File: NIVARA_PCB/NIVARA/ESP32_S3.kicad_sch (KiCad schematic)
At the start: 0 parts

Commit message: SALIDAS DE VOLTAJE Y CORRIENTE
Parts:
- added U11: ESP32-S3-WROOM-1, PCM_Espressif:ESP32-S3-WROOM-1, symbol PCM_Espressif:ESP32-S3-WROOM-1
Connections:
- new net: U11.1 (GND), U11.40 (GND), U11.41 (GND)

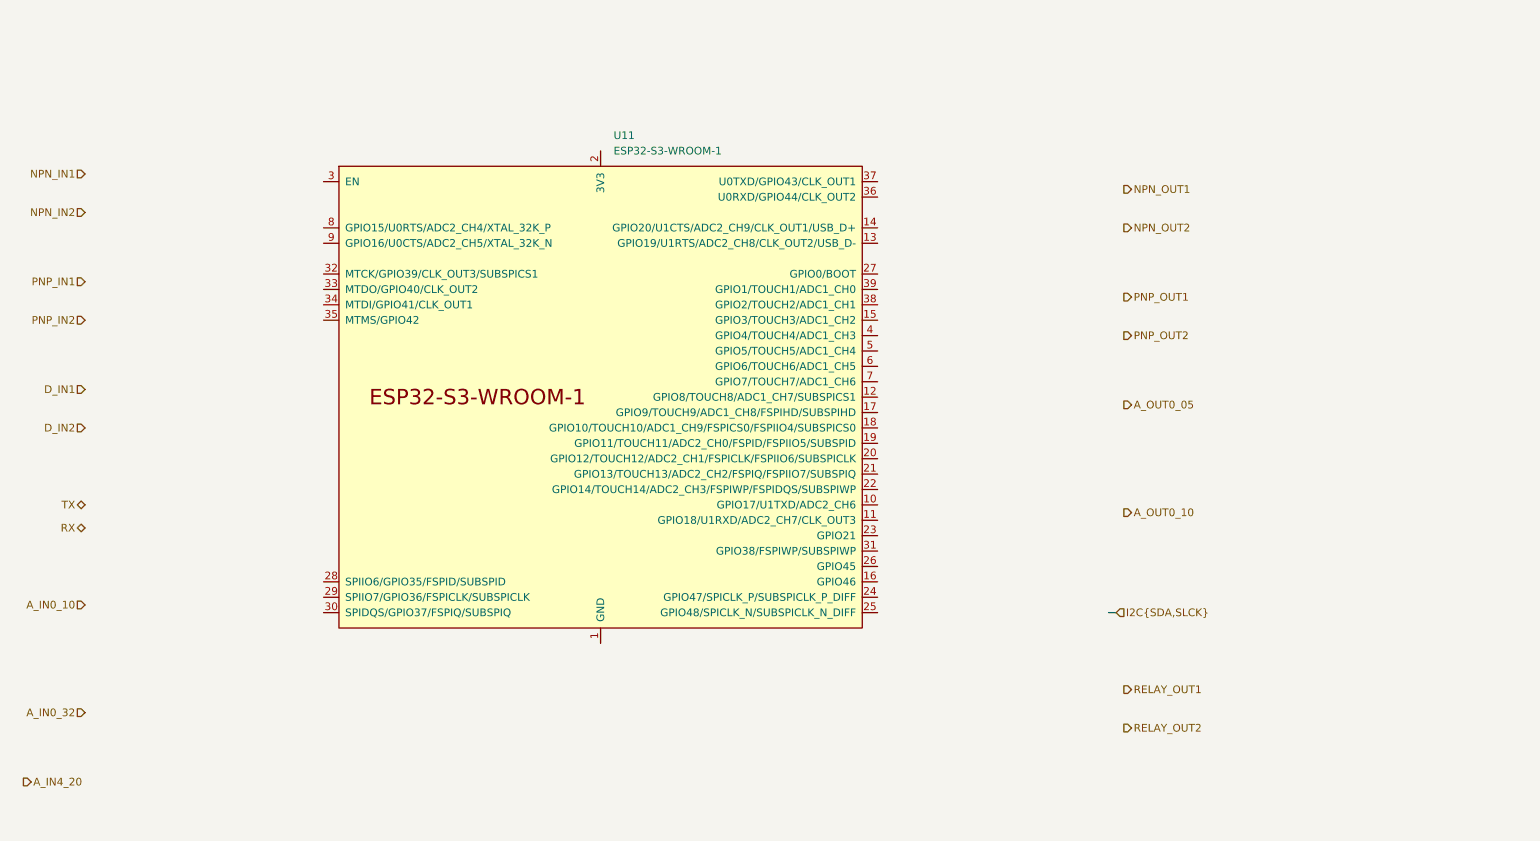
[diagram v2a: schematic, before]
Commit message: Se organizaron componentes en el area de PCB
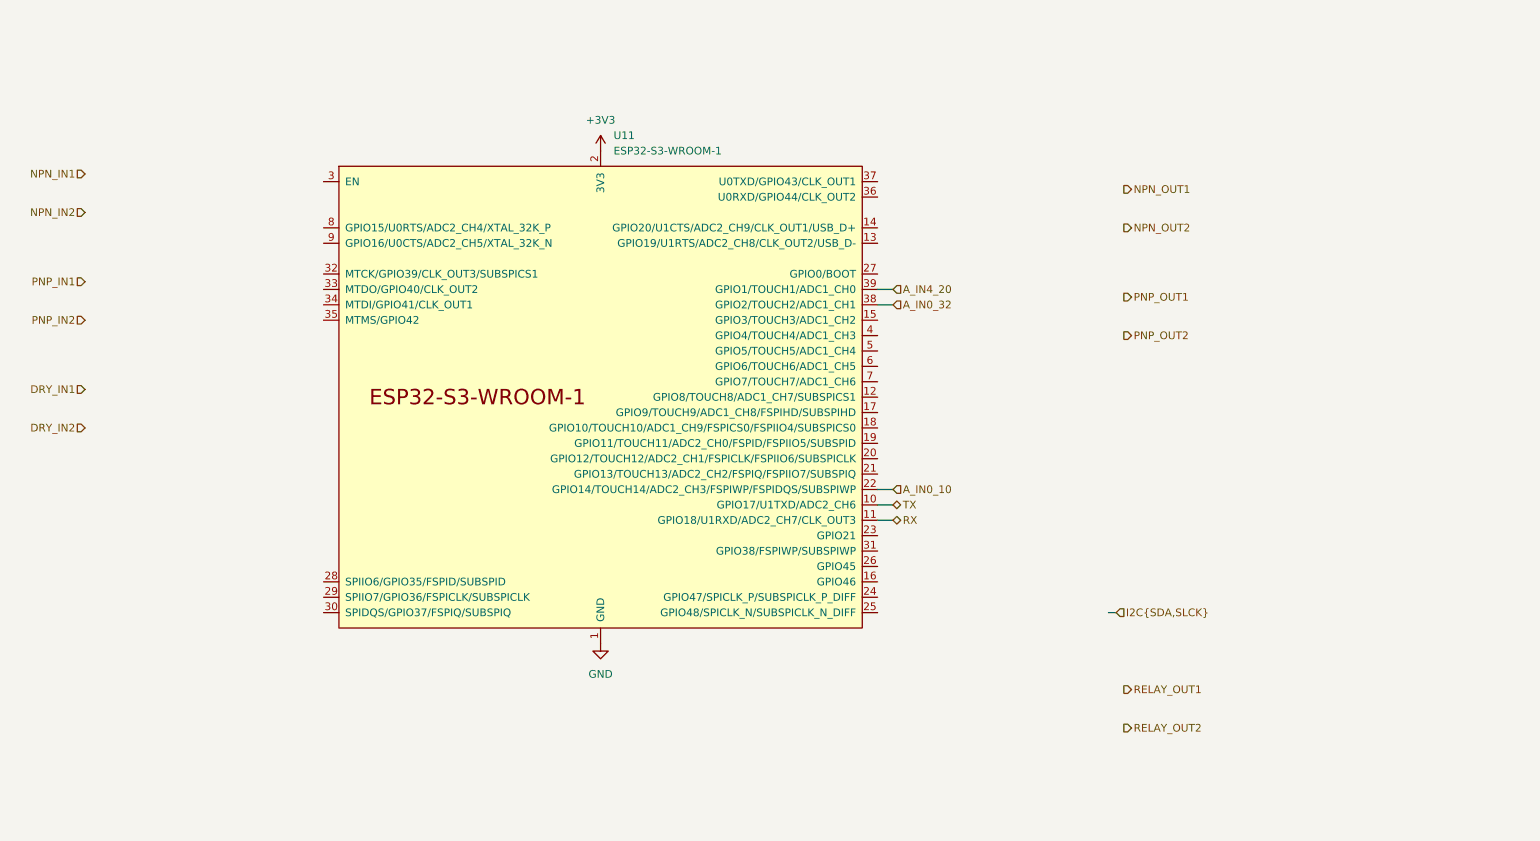
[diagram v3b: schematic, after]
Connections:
- net A_IN0_10: now also U11.22 (GPIO14/TOUCH14/ADC2_CH3/FSPIWP/FSPIDQS/SUBSPIWP)
- net A_IN0_32: now also U11.38 (GPIO2/TOUCH2/ADC1_CH1)
- net A_IN4_20: now also U11.39 (GPIO1/TOUCH1/ADC1_CH0)
- net RX: now also U11.11 (GPIO18/U1RXD/ADC2_CH7/CLK_OUT3)
- net TX: now also U11.10 (GPIO17/U1TXD/ADC2_CH6)
- net GND: now reaches U11.1 (GND), U11.40 (GND), U11.41 (GND)
- net +3V3: now reaches U11.2 (3V3)
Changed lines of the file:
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@@
+		)
+	)
+	(wire
+		(pts
+			(xy 158.75 64.77) (xy 161.29 64.77)
+		)
+		(stroke
+			(width 0)
+			(type default)
+		)
+	)
+	(wire
+		(pts
+			(xy 158.75 97.79) (xy 161.29 97.79)
+		)
+		(stroke
+			(width 0)
+			(type default)
+		)
+	)
+	(wire
+		(pts
+			(xy 158.75 100.33) (xy 161.29 100.33)
+		)
+		(stroke
+			(width 0)
+			(type default)
+		)
+	)
+	(wire
+		(pts
+			(xy 158.75 102.87) (xy 161.29 102.87)
+		)
+		(stroke
+			(width 0)
+			(type default)
+		)
+	)
+	(wire
+		(pts
+			(xy 158.75 67.31) (xy 161.29 67.31)
+		)
+		(stroke
+			(width 0)
+			(type default)
 		)
 	)
@@
 		)
 	)
-	(hierarchical_label "D_IN2"
+	(hierarchical_label "DRY_IN2"
 		(shape input)
 		(at 27.94 87.63 180)
@@
 	(hierarchical_label "RX"
 		(shape bidirectional)
-		(at 27.94 104.14 180)
-		(effects
-			(font
-				(size 1.27 1.27)
-			)
-			(justify right)
+		(at 161.29 102.87 0)
+		(effects
+			(font
+				(size 1.27 1.27)
+			)
+			(justify left)
 		)
 	)
 	(hierarchical_label "A_IN4_20"
-		(shape output)
-		(at 17.78 146.05 0)
+		(shape input)
+		(at 161.29 64.77 0)
 		(effects
 			(font
@@
 		)
 	)
-	(hierarchical_label "A_OUT0_05"
-		(shape output)
-		(at 199.39 83.82 0)
-		(effects
-			(font
-				(size 1.27 1.27)
-			)
-			(justify left)
-		)
-	)
 	(hierarchical_label "NPN_IN1"
 		(shape input)
@@
 		)
 	)
-	(hierarchical_label "A_OUT0_10"
-		(shape output)
-		(at 199.39 101.6 0)
-		(effects
-			(font
-				(size 1.27 1.27)
-			)
-			(justify left)
-		)
-	)
 	(hierarchical_label "RELAY_OUT1"
 		(shape output)
@@
 	(hierarchical_label "A_IN0_32"
 		(shape input)
-		(at 27.94 134.62 180)
-		(effects
-			(font
-				(size 1.27 1.27)
-			)
-			(justify right)
+		(at 161.29 67.31 0)
+		(effects
+			(font
+				(size 1.27 1.27)
+			)
+			(justify left)
 		)
 	)
@@
 		)
 	)
-	(hierarchical_label "D_IN1"
+	(hierarchical_label "DRY_IN1"
 		(shape input)
 		(at 27.94 81.28 180)
@@
 	(hierarchical_label "A_IN0_10"
 		(shape input)
-		(at 27.94 116.84 180)
-		(effects
-			(font
-				(size 1.27 1.27)
-			)
-			(justify right)
+		(at 161.29 97.79 0)
+		(effects
+			(font
+				(size 1.27 1.27)
+			)
+			(justify left)
 		)
 	)
 	(hierarchical_label "TX"
 		(shape bidirectional)
-		(at 27.94 100.33 180)
-		(effects
-			(font
-				(size 1.27 1.27)
-			)
-			(justify right)
+		(at 161.29 100.33 0)
+		(effects
+			(font
+				(size 1.27 1.27)
+			)
+			(justify left)
 		)
 	)
@@
 					(unit 1)
 				)
+			)
+		)
+	)
+	(symbol
+		(lib_id "power:+3V3")
+		(at 113.03 41.91 0)
+		(unit 1)
+		(exclude_from_sim no)
+		(in_bom yes)
+		(on_board yes)
+		(dnp no)
+		(fields_autoplaced yes)
+		(property "Reference" "#PWR02"
+			(at 113.03 45.72 0)
+			(effects
+				(font
+					(size 1.27 1.27)
+				)
+				(hide yes)
+			)
+		)
+		(property "Value" "+3V3"
+			(at 113.03 36.83 0)
+			(effects
+				(font
+					(size 1.27 1.27)
+				)
+			)
+		)
+		(property "Footprint" ""
+			(at 113.03 41.91 0)
+			(effects
+				(font
+					(size 1.27 1.27)
+				)
+				(hide yes)
+			)
+		)
+		(property "Datasheet" ""
+			(at 113.03 41.91 0)
+			(effects
+				(font
+					(size 1.27 1.27)
+				)
+				(hide yes)
+			)
+		)
+		(property "Description" "Power symbol creates a global label with name \"+3V3\""
+			(at 113.03 41.91 0)
+			(effects
+				(font
+					(size 1.27 1.27)
+				)
+				(hide yes)
+			)
+		)
+		(pin "1"
+		)
+		(instances
+			(project ""
+				(path "/6298d7d5-28da-40bf-9586-24a8e5c02b82/7ff0dada-fc46-483c-91ad-b264be8c64cf/f3254285-1e0e-4dcc-8694-b92c90374f4d"
+					(reference "#PWR02")
+					(unit 1)
+				)
+			)
+		)
+	)
+	(symbol
+		(lib_id "power:GND")
+		(at 113.03 123.19 0)
+		(unit 1)
+		(exclude_from_sim no)
+		(in_bom yes)
+		(on_board yes)
+		(dnp no)
+		(fields_autoplaced yes)
+		(property "Reference" "#PWR086"
+			(at 113.03 129.54 0)
+			(effects
+				(font
+					(size 1.27 1.27)
+				)
+				(hide yes)
+			)
+		)
+		(property "Value" "GND"
+			(at 113.03 128.27 0)
+			(effects
+				(font
+					(size 1.27 1.27)
+				)
+			)
+		)
+		(property "Footprint" ""
+			(at 113.03 123.19 0)
+			(effects
+				(font
+					(size 1.27 1.27)
+				)
+				(hide yes)
+			)
+		)
+		(property "Datasheet" ""
+			(at 113.03 123.19 0)
+			(effects
+				(font
+					(size 1.27 1.27)
+				)
+				(hide yes)
+			)
+		)
+		(property "Description" "Power symbol creates a global label with name \"GND\" , ground"
+			(at 113.03 123.19 0)
+			(effects
+				(font
+					(size 1.27 1.27)
+				)
+				(hide yes)
+			)
+		)
+		(pin "1"
+		)
+		(instances
+			(project ""
+				(path "/6298d7d5-28da-40bf-9586-24a8e5c02b82/7ff0dada-fc46-483c-91ad-b264be8c64cf/f3254285-1e0e-4dcc-8694-b92c90374f4d"
+					(reference "#PWR086")
+					(unit 1)
+				)

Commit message: ACTUALIZACION DE SALIDAS NPN Y PNP
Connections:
- net RELAY_OUT1: now also U11.15 (GPIO3/TOUCH3/ADC1_CH2)
- net RELAY_OUT2: now also U11.16 (GPIO46)
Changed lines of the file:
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@@
 	(generator_version "9.0")
 	(paper "A4")
+	(wire
+		(pts
+			(xy 158.75 64.77) (xy 161.29 64.77)
+		)
+		(stroke
+			(width 0)
+			(type default)
+		)
+	)
+	(wire
+		(pts
+			(xy 158.75 97.79) (xy 161.29 97.79)
+		)
+		(stroke
+			(width 0)
+			(type default)
+		)
+	)
+	(wire
+		(pts
+			(xy 158.75 100.33) (xy 161.29 100.33)
+		)
+		(stroke
+			(width 0)
+			(type default)
+		)
+	)
 	(bus
 		(pts
-			(xy 198.12 118.11) (xy 196.85 118.11)
-		)
-		(stroke
-			(width 0)
-			(type default)
-		)
-	)
-	(wire
-		(pts
-			(xy 158.75 64.77) (xy 161.29 64.77)
-		)
-		(stroke
-			(width 0)
-			(type default)
-		)
-	)
-	(wire
-		(pts
-			(xy 158.75 97.79) (xy 161.29 97.79)
-		)
-		(stroke
-			(width 0)
-			(type default)
-		)
-	)
-	(wire
-		(pts
-			(xy 158.75 100.33) (xy 161.29 100.33)
+			(xy 162.56 85.09) (xy 176.53 85.09)
 		)
 		(stroke
@@
 		(pts
 			(xy 158.75 102.87) (xy 161.29 102.87)
+		)
+		(stroke
+			(width 0)
+			(type default)
+		)
+	)
+	(wire
+		(pts
+			(xy 158.75 113.03) (xy 162.56 113.03)
+		)
+		(stroke
+			(width 0)
+			(type default)
+		)
+	)
+	(wire
+		(pts
+			(xy 158.75 69.85) (xy 161.29 69.85)
+		)
+		(stroke
+			(width 0)
+			(type default)
+		)
+	)
+	(bus
+		(pts
+			(xy 162.56 88.9) (xy 162.56 85.09)
 		)
 		(stroke
@@
 	(hierarchical_label "RELAY_OUT2"
 		(shape output)
-		(at 199.39 137.16 0)
+		(at 162.56 113.03 0)
 		(effects
 			(font
@@
 	(hierarchical_label "I2C{SDA,SLCK}"
 		(shape input)
-		(at 198.12 118.11 0)
+		(at 176.53 85.09 0)
 		(fields_autoplaced yes)
 		(effects
@@
 		)
 		(property "I2C" ""
-			(at 198.12 119.38 0)
+			(at 176.53 86.36 0)
 			(effects
 				(font
@@
 	(hierarchical_label "RELAY_OUT1"
 		(shape output)
-		(at 199.39 130.81 0)
-		(effects
-			(font
+		(at 161.29 69.85 0)
+		(effects
+			(font

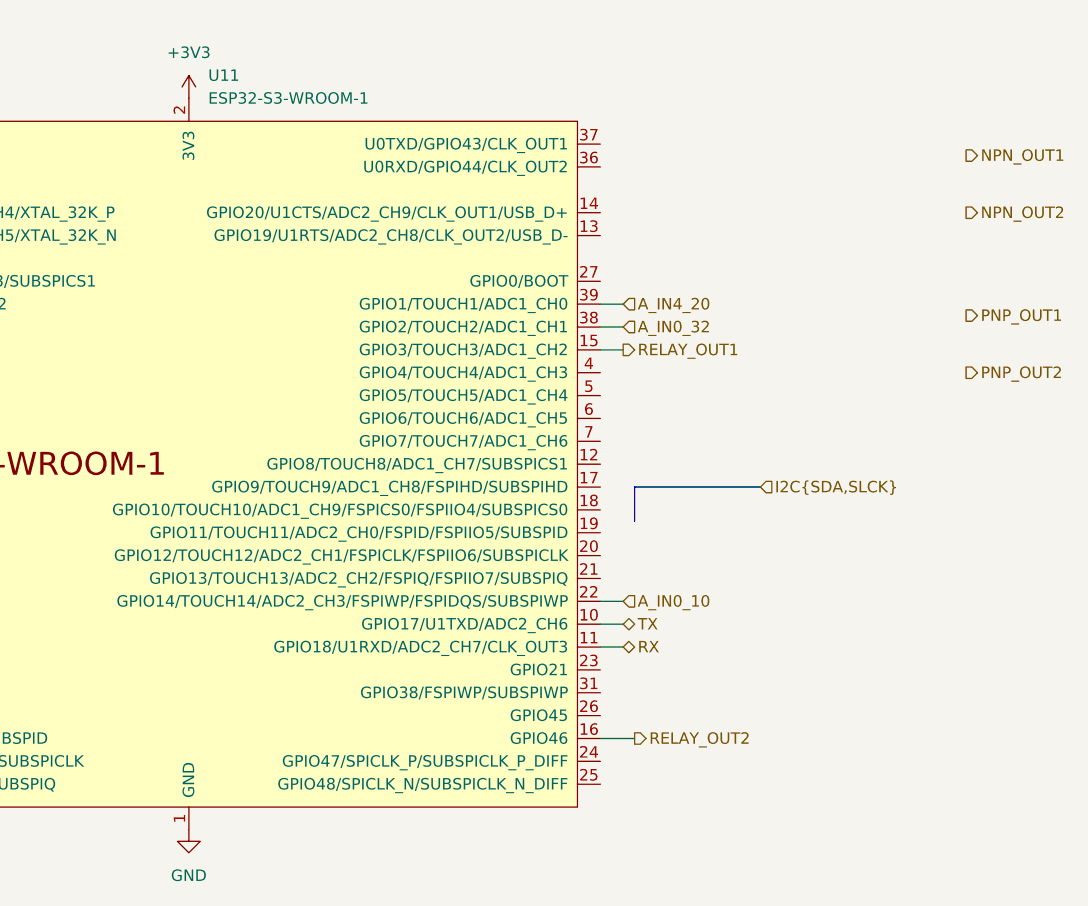
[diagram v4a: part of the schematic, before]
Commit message: arreglo del desastre que tenia con las salidas PNP
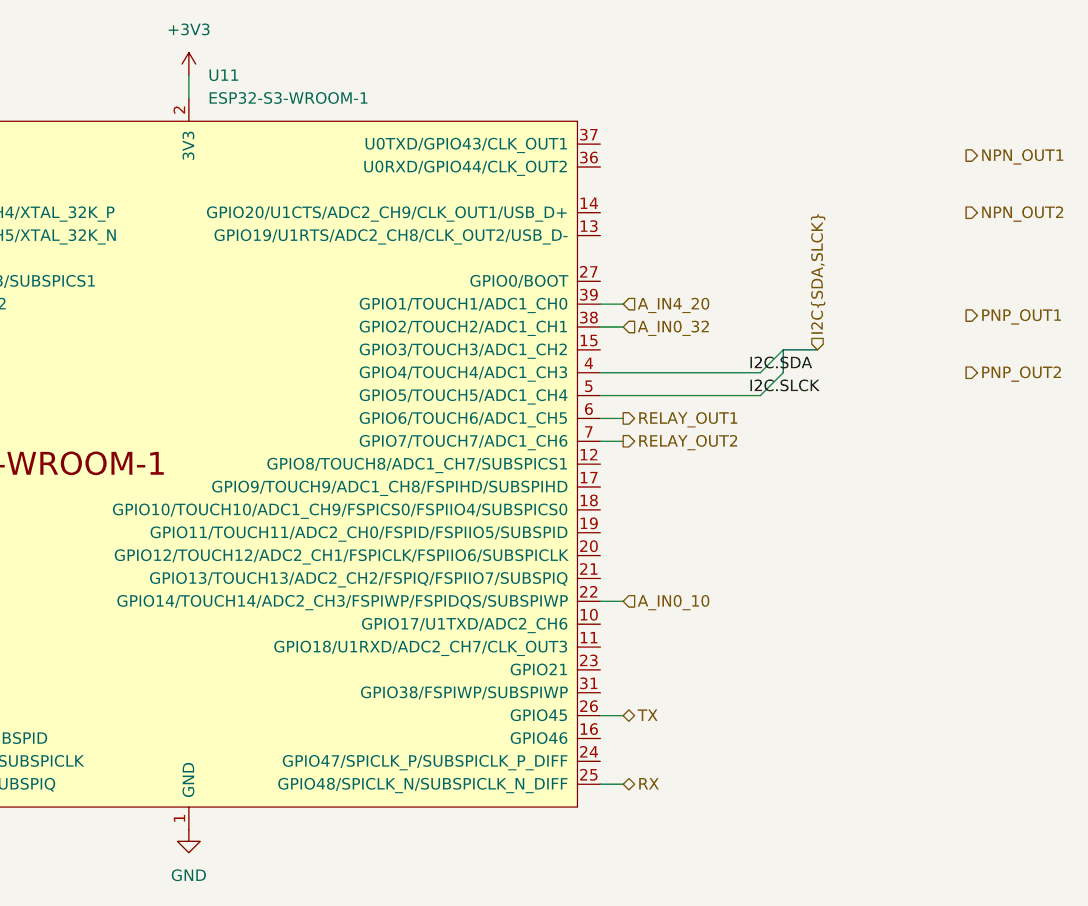
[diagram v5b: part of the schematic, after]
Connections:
- net RELAY_OUT1: now also U11.6 (GPIO6/TOUCH6/ADC1_CH5); no longer U11.15 (GPIO3/TOUCH3/ADC1_CH2)
- net RELAY_OUT2: now also U11.7 (GPIO7/TOUCH7/ADC1_CH6); no longer U11.16 (GPIO46)
- net RX: now also U11.25 (GPIO48/SPICLK_N/SUBSPICLK_N_DIFF); no longer U11.11 (GPIO18/U1RXD/ADC2_CH7/CLK_OUT3)
- net TX: now also U11.26 (GPIO45); no longer U11.10 (GPIO17/U1TXD/ADC2_CH6)
- net I2C.SDA: now reaches U11.4 (GPIO4/TOUCH4/ADC1_CH3)
- net I2C.SLCK: now reaches U11.5 (GPIO5/TOUCH5/ADC1_CH4)
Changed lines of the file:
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@@
 	(generator_version "9.0")
 	(paper "A4")
+	(bus_entry
+		(at 179.07 69.85)
+		(size -2.54 2.54)
+		(stroke
+			(width 0)
+			(type default)
+		)
+	)
+	(bus_entry
+		(at 179.07 72.39)
+		(size -2.54 2.54)
+		(stroke
+			(width 0)
+			(type default)
+		)
+	)
 	(wire
 		(pts
@@
 	(wire
 		(pts
+			(xy 158.75 74.93) (xy 176.53 74.93)
+		)
+		(stroke
+			(width 0)
+			(type default)
+		)
+	)
+	(wire
+		(pts
 			(xy 158.75 97.79) (xy 161.29 97.79)
 		)
@@
 	(wire
 		(pts
-			(xy 158.75 100.33) (xy 161.29 100.33)
+			(xy 158.75 80.01) (xy 161.29 80.01)
+		)
+		(stroke
+			(width 0)
+			(type default)
+		)
+	)
+	(wire
+		(pts
+			(xy 158.75 72.39) (xy 176.53 72.39)
+		)
+		(stroke
+			(width 0)
+			(type default)
+		)
+	)
+	(wire
+		(pts
+			(xy 158.75 77.47) (xy 161.29 77.47)
+		)
+		(stroke
+			(width 0)
+			(type default)
+		)
+	)
+	(wire
+		(pts
+			(xy 161.29 110.49) (xy 158.75 110.49)
 		)
 		(stroke
@@
 	(bus
 		(pts
-			(xy 162.56 85.09) (xy 176.53 85.09)
-		)
-		(stroke
-			(width 0)
-			(type default)
-		)
-	)
-	(wire
-		(pts
-			(xy 158.75 102.87) (xy 161.29 102.87)
-		)
-		(stroke
-			(width 0)
-			(type default)
-		)
-	)
-	(wire
-		(pts
-			(xy 158.75 113.03) (xy 162.56 113.03)
-		)
-		(stroke
-			(width 0)
-			(type default)
-		)
-	)
-	(wire
-		(pts
-			(xy 158.75 69.85) (xy 161.29 69.85)
+			(xy 179.07 69.85) (xy 179.07 72.39)
+		)
+		(stroke
+			(width 0)
+			(type default)
+		)
+	)
+	(wire
+		(pts
+			(xy 113.03 39.37) (xy 113.03 41.91)
+		)
+		(stroke
+			(width 0)
+			(type default)
+		)
+	)
+	(wire
+		(pts
+			(xy 161.29 118.11) (xy 158.75 118.11)
 		)
 		(stroke
@@
 	(bus
 		(pts
-			(xy 162.56 88.9) (xy 162.56 85.09)
+			(xy 179.07 69.85) (xy 182.88 69.85)
 		)
 		(stroke
@@
 			(width 0)
 			(type default)
+		)
+	)
+	(label "I2C.SLCK"
+		(at 175.26 74.93 0)
+		(effects
+			(font
+				(size 1.27 1.27)
+			)
+			(justify left bottom)
+		)
+	)
+	(label "I2C.SDA"
+		(at 175.26 72.39 0)
+		(effects
+			(font
+				(size 1.27 1.27)
+			)
+			(justify left bottom)
 		)
 	)
@@
 	(hierarchical_label "RX"
 		(shape bidirectional)
-		(at 161.29 102.87 0)
+		(at 161.29 118.11 0)
+		(effects
+			(font
+				(size 1.27 1.27)
+			)
+			(justify left)
+		)
+	)
+	(hierarchical_label "TX"
+		(shape bidirectional)
+		(at 161.29 110.49 0)
+		(effects
+			(font
+				(size 1.27 1.27)
+			)
+			(justify left)
+		)
+	)
+	(hierarchical_label "RELAY_OUT1"
+		(shape output)
+		(at 161.29 77.47 0)
 		(effects
 			(font
@@
 	(hierarchical_label "RELAY_OUT2"
 		(shape output)
-		(at 162.56 113.03 0)
-		(effects
-			(font
-				(size 1.27 1.27)
-			)
-			(justify left)
-		)
-	)
-	(hierarchical_label "I2C{SDA,SLCK}"
-		(shape input)
-		(at 176.53 85.09 0)
-		(fields_autoplaced yes)
-		(effects
-			(font
-				(size 1.27 1.27)
-			)
-			(justify left)
-		)
-		(property "I2C" ""
-			(at 176.53 86.36 0)
-			(effects
-				(font
-					(size 1.27 1.27)
-					(italic yes)
-				)
-				(justify left)
-			)
+		(at 161.29 80.01 0)
+		(effects
+			(font
+				(size 1.27 1.27)
+			)
+			(justify left)
 		)
 	)
@@
 		)
 	)
-	(hierarchical_label "RELAY_OUT1"
-		(shape output)
-		(at 161.29 69.85 0)
-		(effects
-			(font
-				(size 1.27 1.27)
-			)
-			(justify left)
-		)
-	)
 	(hierarchical_label "A_IN0_32"
 		(shape input)
@@
 			)
 			(justify left)
+		)
+	)
+	(hierarchical_label "I2C{SDA,SLCK}"
+		(shape input)
+		(at 182.88 69.85 90)
+		(fields_autoplaced yes)
+		(effects
+			(font
+				(size 1.27 1.27)
+			)
+			(justify left)
+		)
+		(property "I2C" ""
+			(at 184.15 69.85 90)
+			(effects
+				(font
+					(size 1.27 1.27)
+					(italic yes)
+				)
+				(justify left)
+			)
 		)
 	)
@@
 		(shape input)
 		(at 161.29 97.79 0)
-		(effects
-			(font
-				(size 1.27 1.27)
-			)
-			(justify left)
-		)
-	)
-	(hierarchical_label "TX"
-		(shape bidirectional)
-		(at 161.29 100.33 0)
 		(effects
 			(font
@@
 	(symbol
 		(lib_id "power:+3V3")
-		(at 113.03 41.91 0)
+		(at 113.03 39.37 0)
 		(unit 1)
 		(exclude_from_sim no)
@@
 		(fields_autoplaced yes)
 		(property "Reference" "#PWR02"
-			(at 113.03 45.72 0)
+			(at 113.03 43.18 0)
 			(effects
 				(font
@@
 		)
 		(property "Value" "+3V3"
-			(at 113.03 36.83 0)
+			(at 113.03 34.29 0)
 			(effects
 				(font
@@
 		)
 		(property "Footprint" ""
-			(at 113.03 41.91 0)
+			(at 113.03 39.37 0)
 			(effects
 				(font
@@
 		)
 		(property "Datasheet" ""
-			(at 113.03 41.91 0)
+			(at 113.03 39.37 0)
 			(effects
 				(font
@@
 		)
 		(property "Description" "Power symbol creates a global label with name \"+3V3\""
-			(at 113.03 41.91 0)
-			(effects
-				(font
+			(at 113.03 39.37 0)
+			(effects
+				(font

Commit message: ruteo de salidas
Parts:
- added C23, C24, C25: 100nF, PCM_Capacitor_SMD_AKL:C_0603_1608Metric, symbol PCM_Capacitor_AKL:C_0603
- added R42, R45: 2.5K, PCM_Resistor_SMD_AKL:R_0603_1608Metric, symbol PCM_Resistor_AKL:R_0603
- added R46, R47: 10K, PCM_Resistor_SMD_AKL:R_0603_1608Metric, symbol PCM_Resistor_AKL:R_0603
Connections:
- net +3V3: now also C23.2, C24.2, R42.1, R45.1, R46.1, R47.1
- net GND: now also C23.1, C24.1, C25.1
- net I2C.SDA: now also R42.2
- net I2C.SLCK: now also R45.2
- net NPN_OUT1: now also U11.10 (GPIO17/U1TXD/ADC2_CH6)
- net NPN_OUT2: now also U11.11 (GPIO18/U1RXD/ADC2_CH7/CLK_OUT3)
- net PNP_OUT1: now also U11.8 (GPIO15/U0RTS/ADC2_CH4/XTAL_32K_P)
- net PNP_OUT2: now also U11.7 (GPIO7/TOUCH7/ADC1_CH6)
- net RELAY_OUT2: now also U11.9 (GPIO16/U0CTS/ADC2_CH5/XTAL_32K_N); no longer U11.7 (GPIO7/TOUCH7/ADC1_CH6)
- net RX: no longer U11.25 (GPIO48/SPICLK_N/SUBSPICLK_N_DIFF)
- net TX: no longer U11.26 (GPIO45)
- net BOOT: now reaches U11.27 (GPIO0/BOOT)
- net BOOT: now also R47.2
- net EN: now reaches U11.3 (EN)
- net EN: now also C25.2, R46.2
